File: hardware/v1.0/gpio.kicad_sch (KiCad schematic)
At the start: 23 parts, among them J2 HDMI_C_1.3, U1 ECP5U_12_CABGA256, U5 PCA9306DC1

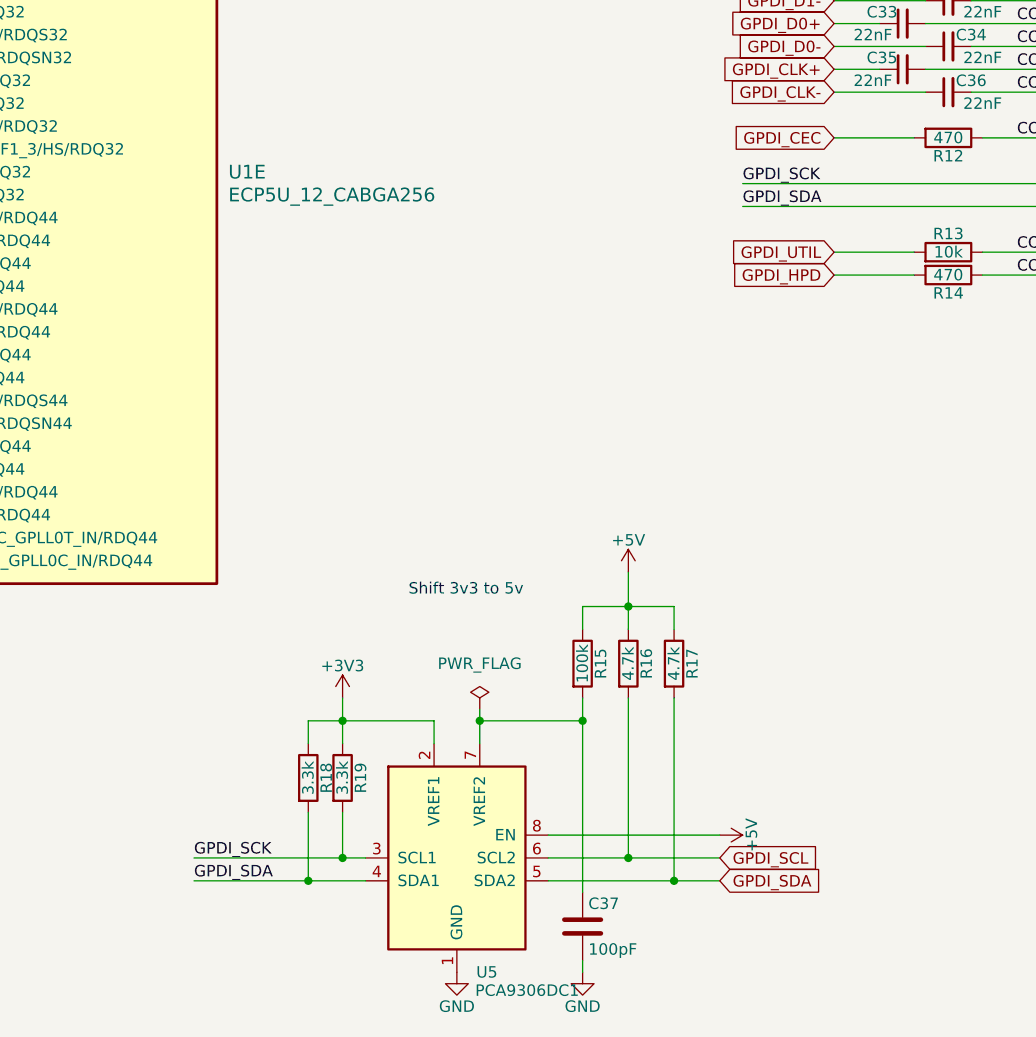
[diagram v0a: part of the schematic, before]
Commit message: Increase pad spacing to 1.9mm and change SCL name to SCK
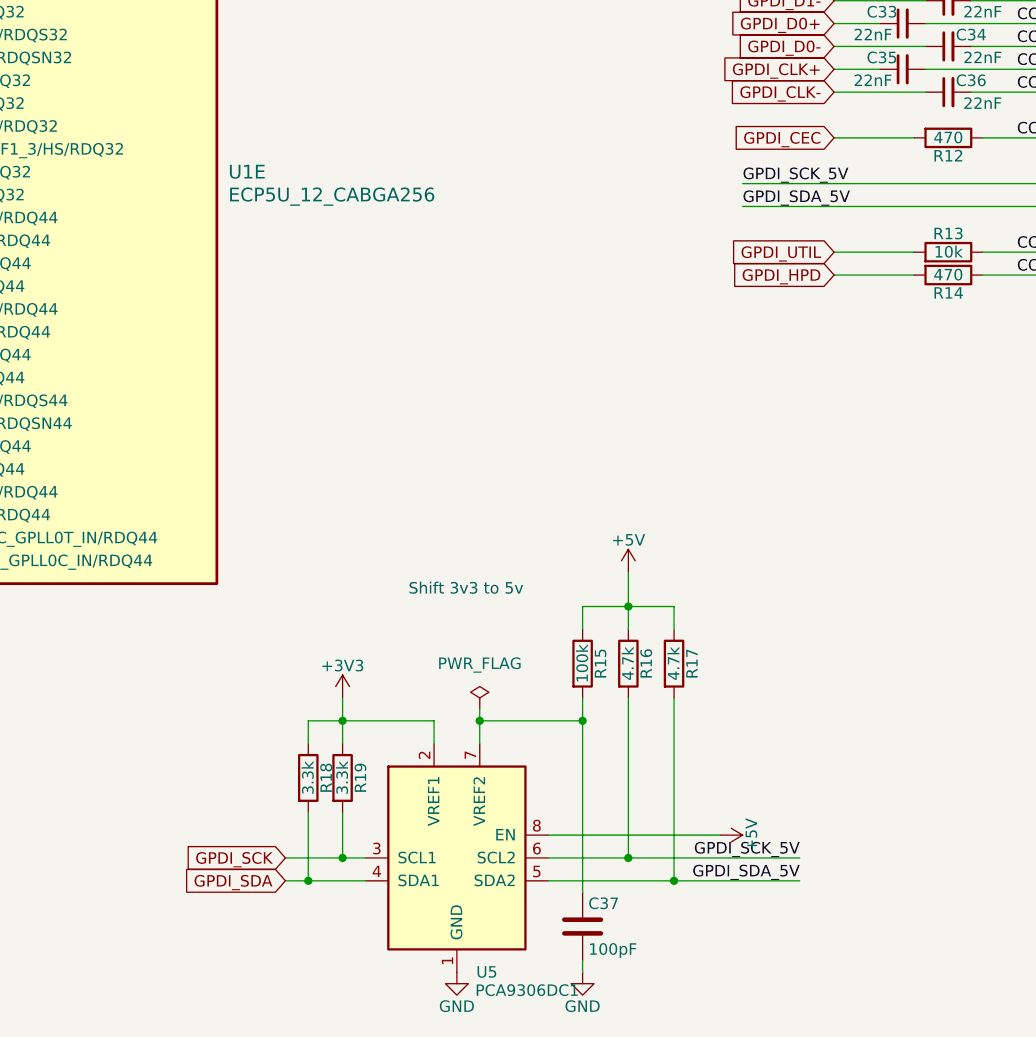
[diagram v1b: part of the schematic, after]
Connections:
- net GPDI_SCK: no longer J2.15 (SCL)
- net GPDI_SDA: no longer J2.16 (SDA), R17.2, U5.5 (SDA2)
- net GPDI_SCL renamed GPDI_SCK_5V
- net GPDI_SCK_5V: now also J2.15 (SCL)
- new net GPDI_SDA_5V: J2.16 (SDA), R17.2, U5.5 (SDA2)
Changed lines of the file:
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@@
+	)
+	(junction
+		(at 113.03 176.53)
+		(diameter 0)
+		(color 0 0 0 0)
 	)
 	(junction
@@
 	)
 	(junction
+		(at 116.84 173.99)
+		(diameter 0)
+		(color 0 0 0 0)
+	)
+	(junction
 		(at 91.44 45.72)
 		(diameter 0)
@@
 	(junction
 		(at 80.01 45.72)
-		(diameter 0)
-		(color 0 0 0 0)
-	)
-	(junction
-		(at 113.03 176.53)
-		(diameter 0)
-		(color 0 0 0 0)
-	)
-	(junction
-		(at 116.84 173.99)
 		(diameter 0)
 		(color 0 0 0 0)
@@
 	(wire
 		(pts
-			(xy 148.59 173.99) (xy 158.75 173.99)
-		)
-		(stroke
-			(width 0)
-			(type default)
-		)
-	)
-	(wire
-		(pts
 			(xy 161.29 101.6) (xy 203.2 101.6)
 		)
@@
 	(wire
 		(pts
-			(xy 153.67 176.53) (xy 158.75 176.53)
+			(xy 153.67 176.53) (xy 167.64 176.53)
 		)
 		(stroke
@@
 	(wire
 		(pts
-			(xy 100.33 173.99) (xy 116.84 173.99)
+			(xy 148.59 173.99) (xy 167.64 173.99)
 		)
 		(stroke
@@
 	(wire
 		(pts
+			(xy 110.49 173.99) (xy 116.84 173.99)
+		)
+		(stroke
+			(width 0)
+			(type default)
+		)
+	)
+	(wire
+		(pts
 			(xy 91.44 45.72) (xy 91.44 46.99)
 		)
@@
 	(wire
 		(pts
+			(xy 110.49 176.53) (xy 113.03 176.53)
+		)
+		(stroke
+			(width 0)
+			(type default)
+		)
+	)
+	(wire
+		(pts
 			(xy 171.45 71.12) (xy 176.53 71.12)
 		)
@@
 		)
 	)
-	(wire
-		(pts
-			(xy 100.33 176.53) (xy 113.03 176.53)
-		)
-		(stroke
-			(width 0)
-			(type default)
-		)
-	)
-	(label "GPDI_SCK"
-		(at 100.33 173.99 0)
-		(effects
-			(font
-				(size 1.27 1.27)
-			)
-			(justify left bottom)
+	(label "GPDI_SCK_5V"
+		(at 167.64 173.99 180)
+		(effects
+			(font
+				(size 1.27 1.27)
+			)
+			(justify right bottom)
 		)
 	)
@@
 		)
 	)
-	(label "GPDI_SDA"
+	(label "GPDI_SDA_5V"
 		(at 161.29 101.6 0)
 		(effects
@@
 		)
 	)
-	(label "GPDI_SDA"
-		(at 100.33 176.53 0)
-		(effects
-			(font
-				(size 1.27 1.27)
-			)
-			(justify left bottom)
+	(label "GPDI_SDA_5V"
+		(at 167.64 176.53 180)
+		(effects
+			(font
+				(size 1.27 1.27)
+			)
+			(justify right bottom)
 		)
 	)
@@
 		)
 	)
-	(label "GPDI_SCK"
+	(label "GPDI_SCK_5V"
 		(at 161.29 99.06 0)
 		(effects
@@
 	(global_label "GPDI_SDA"
 		(shape input)
-		(at 158.75 176.53 0)
-		(effects
-			(font
-				(size 1.27 1.27)
-			)
-			(justify left)
-		)
-		(property "Intersheetrefs" "${INTERSHEET_REFS}"
-			(at 158.75 176.53 0)
+		(at 110.49 176.53 180)
+		(effects
+			(font
+				(size 1.27 1.27)
+			)
+			(justify right)
+		)
+		(property "Intersheetrefs" "${INTERSHEET_REFS}"
+			(at 110.49 176.53 0)
 			(effects
 				(font
@@
 		)
 	)
-	(global_label "GPDI_SCL"
-		(shape input)
-		(at 158.75 173.99 0)
-		(effects
-			(font
-				(size 1.27 1.27)
-			)
-			(justify left)
-		)
-		(property "Intersheetrefs" "${INTERSHEET_REFS}"
-			(at 158.75 173.99 0)
-			(effects
-				(font
+	(global_label "GPDI_SCK"
+		(shape input)
+		(at 110.49 173.99 180)
+		(effects
+			(font
+				(size 1.27 1.27)
+			)
+			(justify right)
+		)
+		(property "Intersheetrefs" "${INTERSHEET_REFS}"
+			(at 110.49 173.99 0)
+			(effects
+				(font

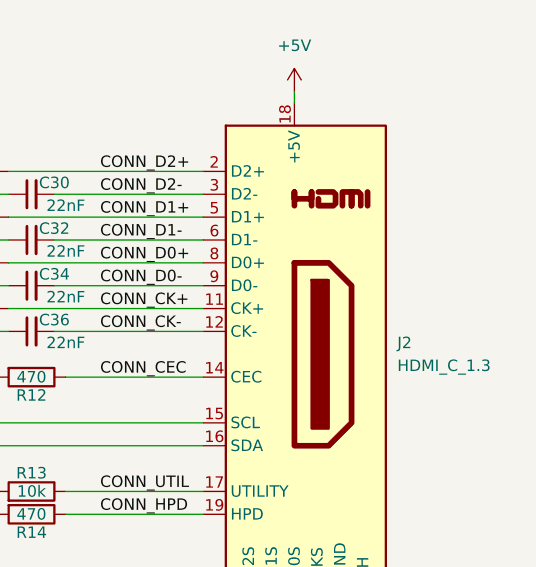
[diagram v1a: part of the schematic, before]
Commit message: Added start of documentation and changed GPDI
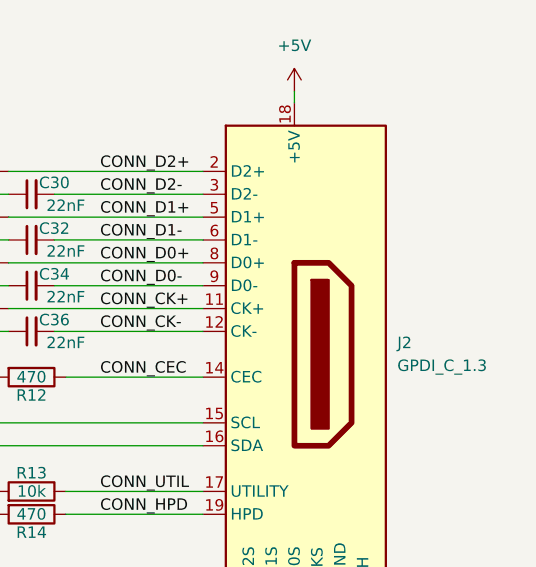
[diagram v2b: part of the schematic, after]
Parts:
- J2: value HDMI_C_1.3 -> GPDI_C_1.3; symbol Connector:HDMI_C_1.3 -> icepi-lib:GPDI_C_1.3; LCSC Link (none) -> https://lcsc.com/product-detail/HDMI-Connectors_XKB-Connect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; Manufactuer Part Number (none) -> A71-05H4-111N1
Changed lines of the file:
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@@
 	)
 	(symbol
-		(lib_id "Connector:HDMI_C_1.3")
+		(lib_id "icepi-lib:GPDI_C_1.3")
 		(at 213.36 91.44 0)
 		(unit 1)
@@
 			)
 		)
-		(property "Value" "HDMI_C_1.3"
+		(property "Value" "GPDI_C_1.3"
 			(at 224.79 92.7099 0)
 			(effects
@@
 			)
 		)
-		(property "Datasheet" "http://pinoutguide.com/PortableDevices/mini_hdmi_pinout.shtml"
+		(property "Datasheet" "-"
 			(at 213.995 91.44 0)
 			(effects
@@
 			)
 		)
-		(property "Description" "HDMI 1.3+ type C connector"
+		(property "Description" "GPDI type C connector"
 			(at 213.36 91.44 0)
 			(effects
@@
 		)
 		(property "LCSC Part #" "C2682170"
+			(at 213.36 91.44 0)
+			(effects
+				(font
+					(size 1.27 1.27)
+				)
+				(hide yes)
+			)
+		)
+		(property "LCSC Link" "https://lcsc.com/product-detail/HDMI-Connectors_XKB-Connection-A71-05H4-111N1_C2682170.html"
+			(at 213.36 91.44 0)
+			(effects
+				(font
+					(size 1.27 1.27)
+				)
+				(hide yes)
+			)
+		)
+		(property "Manufactuer Part Number" "A71-05H4-111N1"
 			(at 213.36 91.44 0)
 			(effects
@@
 		)
 		(instances
-			(project ""
+			(project "icepi-zero"
 				(path "/f88da08e-cf42-4d03-a08f-3f602fe6658d/efe0a411-ae63-4682-aa63-a9a30697cd67"
 					(reference "J2")
